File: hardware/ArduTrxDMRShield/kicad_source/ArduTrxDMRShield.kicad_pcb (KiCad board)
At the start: 2 copper layers, 84.8 x 53 mm, 78 parts, among them CN1 60312202114509, CN2 ARDUINO, CN3 CON_KLINKE3, CN4 CON_KLINKE3, CN5 CONN_01X03, CN6 CONN_01X02, CN7 691322310002, Q2 2N7002, Q3 2N7002, SW1 TAST_HOR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

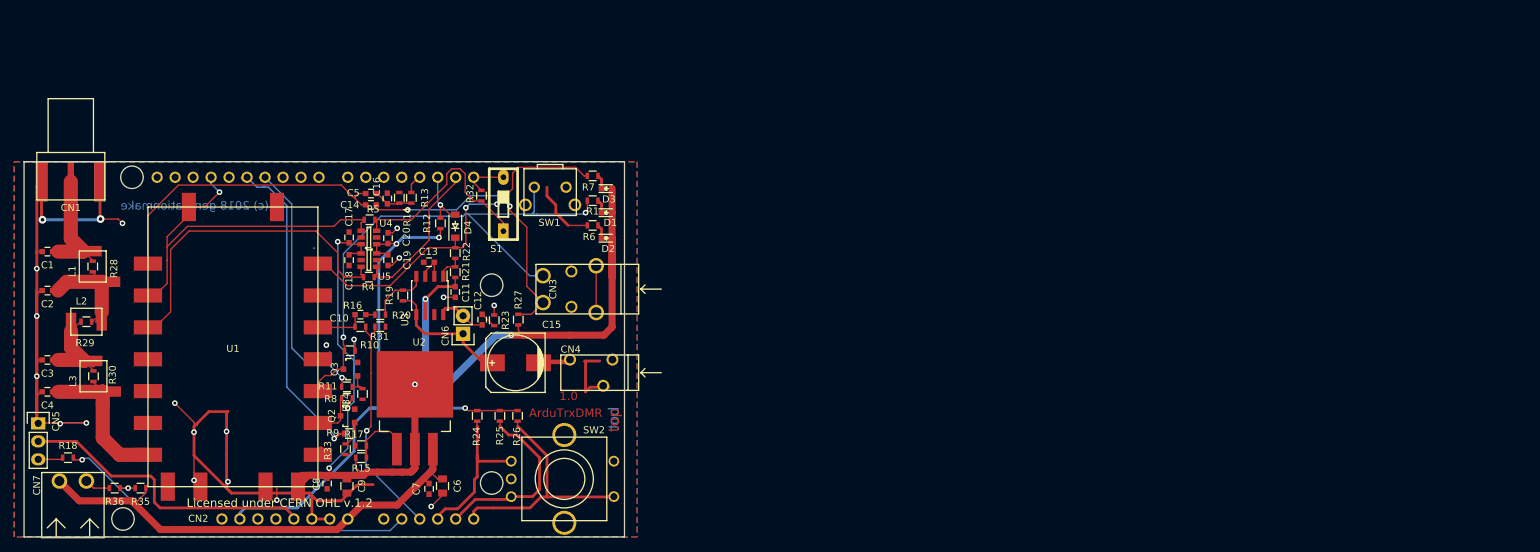
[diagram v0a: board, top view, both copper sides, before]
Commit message: corrected schematic, updated layout
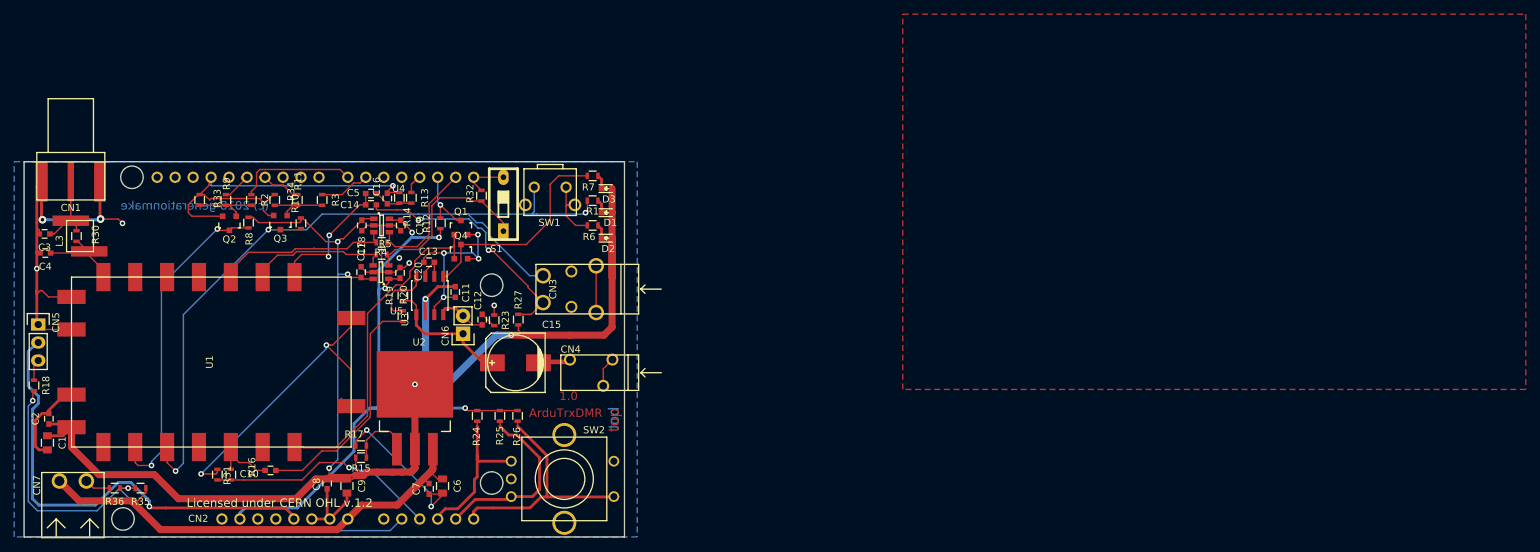
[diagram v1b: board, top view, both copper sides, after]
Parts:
- removed D4: BAT46ZFILM, diodes:SOD-123
- removed L1, L2: 744912156, L_filter:WE-CAIR_4248
- removed R21: 4k7, resistors:R_0603
- removed R22: 100, resistors:R_0603
- removed R28, R29: DNI, resistors:R_0603
- added Q1: 2N7002, SOT_TO:SOT-23, F.Cu at (116.4, 86.3)
- added Q4: 2N7002, SOT_TO:SOT-23, F.Cu at (116.4, 89.7)
- added R2: 100, resistors:R_0603, F.Cu at (86.8, 82.4)
- added R3: 100, resistors:R_0603, F.Cu at (96.8, 82.4)
- C1: value 30p -> 10u; footprint capacitors:C_0603 -> capacitors:C_0805
- C2: value 47p -> 100n
- moved R33 40.8 mm to (79.5, 82.4), turned to 90 degrees
- moved R9 37.3 mm to (83.2, 82.4), turned to 270 degrees
- moved Q2 31.9 mm to (83.7, 85.7), turned to 180 degrees
- moved R31 31.1 mm to (82.0, 121.2), turned to 90 degrees
- moved R34 30.1 mm to (90.1, 82.4), turned to 90 degrees
- moved R8 28.4 mm to (86.4, 85.6), turned to 270 degrees
- moved R16 27.8 mm to (83.9, 121.2), turned to 270 degrees
- moved R11 27.3 mm to (93.3, 82.4), turned to 270 degrees
- moved C1 27.0 mm to (58.0, 116.7), turned to 270 degrees
- moved C10 25.4 mm to (89.5, 120.6)
- moved Q3 22.9 mm to (90.9, 85.6), turned to 180 degrees
- moved R30 19.9 mm to (62.1, 87.5)
- moved L3 19.9 mm to (62.6, 87.5)
- moved C4 19.6 mm to (57.7, 89.9)
- moved R10 19.3 mm to (93.8, 85.7), turned to 270 degrees
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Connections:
- C1 pad 1: /ANT3 -> VCC
- C2 pad 1: /ANT2 -> VCC
- C3 pad 1: /ANT1 -> /ANT3
- CN2 pad 10: (no net) -> /KEYPAD_10
- CN2 pad 11: /PTT_Q -> /PTT_Q_1
- CN2 pad 12: /PD_Q -> /PD_Q_1
- CN2 pad 13: (no net) -> Net-(CN2-Pad13)
- CN2 pad 15: (no net) -> Net-(CN2-Pad15)
- CN2 pad 16: (no net) -> Net-(CN2-Pad16)
- CN2 pad 17: (no net) -> Net-(CN2-Pad17)
- CN2 pad 23: (no net) -> /KEYPAD_A0
- CN2 pad 28: (no net) -> Net-(CN2-Pad28)
- CN2 pad 29: (no net) -> Net-(CN2-Pad29)
- CN2 pad 31: (no net) -> Net-(CN2-Pad31)
- CN2 pad 4: (no net) -> /KEYPAD_4
- CN2 pad 5: (no net) -> /KEYPAD_5
- CN2 pad 6: (no net) -> /PTT_Q_2
- CN2 pad 7: (no net) -> /PD_Q_2
- CN2 pad 8: (no net) -> /KEYPAD_8
- CN2 pad 9: (no net) -> /KEYPAD_9
- L3 pad 1: /ANT1 -> /ANT3
- Q2 pad 1: Net-(Q2-Pad1) -> /PD_Q
- Q3 pad 1: Net-(Q3-Pad1) -> /PTT_Q
- R11 pad 1: /PTT_Q -> /PTT_Q_1
- R11 pad 2: Net-(Q3-Pad1) -> /PTT_Q
- R30 pad 2: /ANT1 -> /ANT3
- R33 pad 1: Net-(Q2-Pad1) -> /PD_Q
- R34 pad 1: Net-(Q3-Pad1) -> /PTT_Q
- R9 pad 1: /PD_Q -> /PD_Q_1
- R9 pad 2: Net-(Q2-Pad1) -> /PD_Q
- U1 pad 12: (no net) -> Net-(U1-Pad12)
- U1 pad 15: (no net) -> Net-(U1-Pad15)
- U1 pad 17: (no net) -> Net-(U1-Pad17)
- U1 pad 18: /SQ -> /SQ_Q
- U1 pad 4: (no net) -> Net-(U1-Pad4)
- U1 pad 5: (no net) -> Net-(U1-Pad5)
- U1 pad 6: (no net) -> Net-(U1-Pad6)
- U3 pad 1: Net-(R21-Pad2) -> /SQ
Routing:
- net GND: track 214.3 -> 285.1 mm, vias 21 -> 16
- net VCC: track 195.6 -> 243.8 mm, vias 7 -> 6
- net /SQ_Q: track 0.00 -> 47.3 mm
- net /PD: track 6.53 -> 46.5 mm, vias 0 -> 2
- net /PD_Q: track 46.5 -> 9.74 mm, vias 1 -> 0
- net /PTT: track 80.8 -> 115.0 mm, vias 2 -> 3
- net Net-(C10-Pad1): track 1.30 -> 33.6 mm
- net /ANT1: track 29.2 -> 0.00 mm
- net /PTT_Q: track 35.9 -> 9.10 mm, vias 1 -> 0
- net /ANT2: track 26.7 -> 0.00 mm
- net /RXD_R: track 44.6 -> 20.0 mm
- net /MIC_IN: track 43.3 -> 19.1 mm, vias 0 -> 2
- net +5V: track 42.3 -> 65.1 mm, vias 0 -> 1
- net /TXD_R: track 47.0 -> 24.8 mm
- net /GPS_RX: track 55.0 -> 77.1 mm
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
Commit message: updated schematic and layout, connected some nets to 3.3v output of DMR818
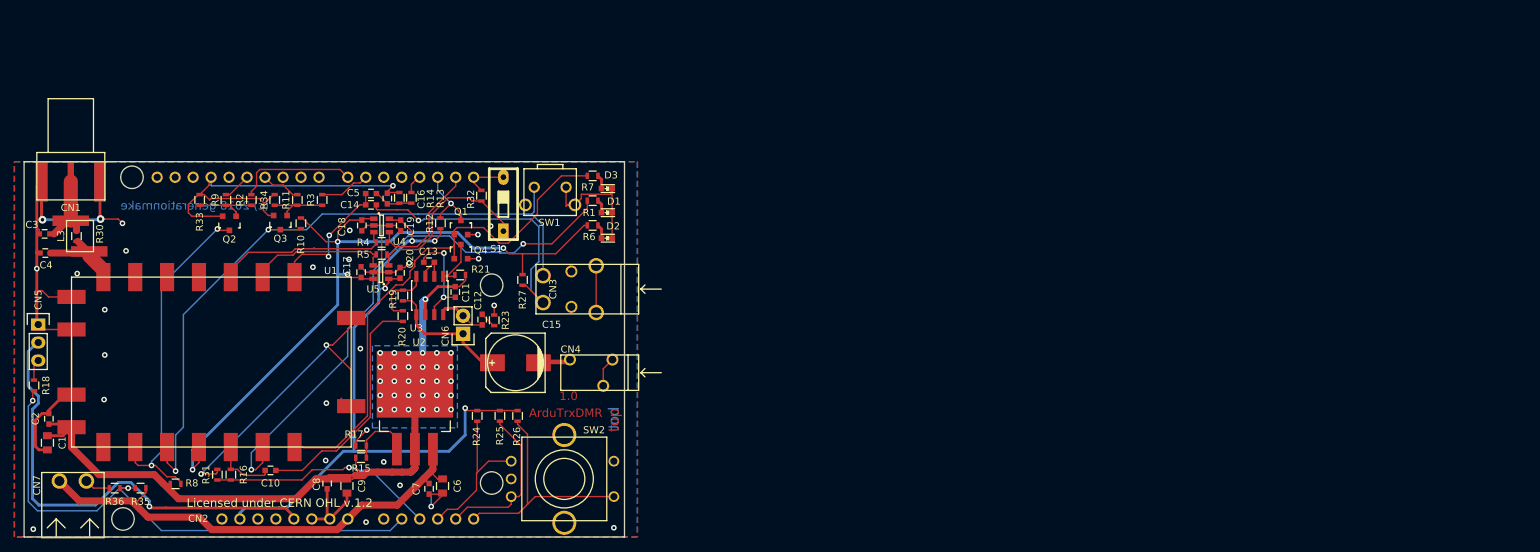
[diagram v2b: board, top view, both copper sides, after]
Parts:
- added R21: 4k7, resistors:R_0603, F.Cu at (116.3, 93.0)
- moved R8 38.3 mm to (76.1, 122.5), turned to 0 degrees
- moved R27 5.63 mm to (125.1, 93.7), turned to 270 degrees
- turned D1 to 180 degrees
- turned D2 to 180 degrees
- turned D3 to 180 degrees
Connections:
- C17 pad 1: VCC -> +3V3
- C18 pad 1: VCC -> +3V3
- D1 pad 1: Net-(D1-Pad1) -> GND
- D1 pad 2: VCC -> Net-(D1-Pad2)
- D2 pad 1: Net-(D2-Pad1) -> GND
- D2 pad 2: VCC -> Net-(D2-Pad2)
- D3 pad 1: Net-(D3-Pad1) -> GND
- D3 pad 2: VCC -> Net-(D3-Pad2)
- R1 pad 1: Net-(D1-Pad1) -> Net-(D1-Pad2)
- R1 pad 2: /PTT -> /TRANSMIT
- R10 pad 1: VCC -> +3V3
- R27 pad 1: VCC -> +3V3
- R6 pad 1: Net-(D2-Pad1) -> Net-(D2-Pad2)
- R6 pad 2: GND -> +3V3
- R7 pad 1: Net-(D3-Pad1) -> Net-(D3-Pad2)
- R7 pad 2: /SQ -> /SQ_Q
- U1 pad 15: Net-(U1-Pad15) -> +3V3
- U1 pad 17: Net-(U1-Pad17) -> /TRANSMIT
- U4 pad 1: VCC -> +3V3
- U5 pad 6: VCC -> +3V3
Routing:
- net VCC: track 243.8 -> 123.6 mm, vias 6 -> 31
- net +3V3: track 0.00 -> 109.8 mm, vias 0 -> 4
- net /TRANSMIT: track 0.00 -> 76.4 mm, vias 0 -> 2
- net /SQ_Q: track 47.3 -> 72.9 mm
- net /SQ: track 30.7 -> 7.54 mm
- net /PTT: track 115.0 -> 99.8 mm, vias 3 -> 2
- net GND: track 285.1 -> 272.7 mm, vias 16 -> 32
- net VIO: track 113.2 -> 101.4 mm
- net /MIC: track 35.3 -> 40.5 mm, vias 2 -> 1
- net /ENC_B: track 26.5 -> 23.1 mm
- net /PD: track 46.5 -> 49.0 mm
- net Net-(D3-Pad2): track 0.00 -> 2.01 mm
- net Net-(D3-Pad1): track 2.01 -> 0.00 mm
- net Net-(D2-Pad2): track 0.00 -> 2.01 mm
- net Net-(D2-Pad1): track 2.01 -> 0.00 mm
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- added copper zone on B.Cu, net VCC
